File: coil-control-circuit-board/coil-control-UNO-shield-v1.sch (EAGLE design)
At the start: 26 parts, among them Q1 IRLML0060, Q2 IRLML0060, SW2 BUTTON, SW3 BUTTON, U2 LM4250, U3 LM4250

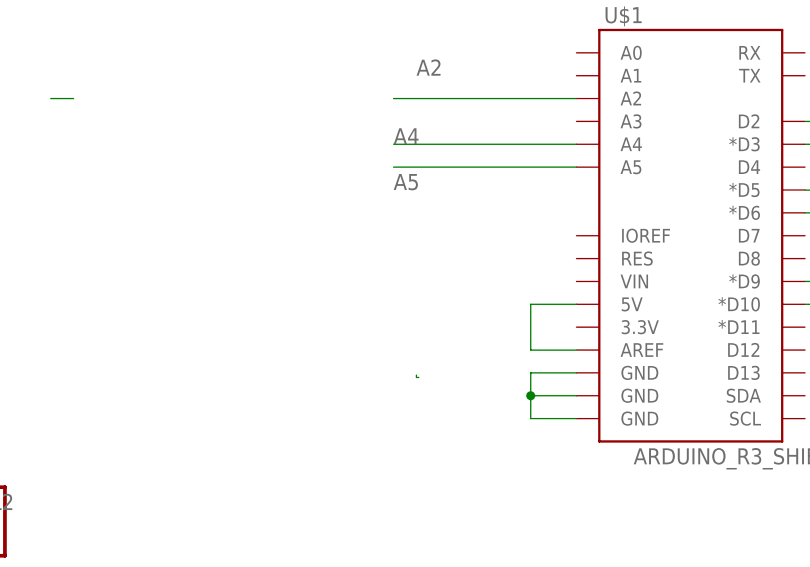
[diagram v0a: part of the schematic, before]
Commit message: finished the boards, mostly
added DC power connector, shifted everything over to work on the Yun(
make space for the big connectors), connected Vin to the input DC
power, cleaned stuff up a bit, moved stuff around.
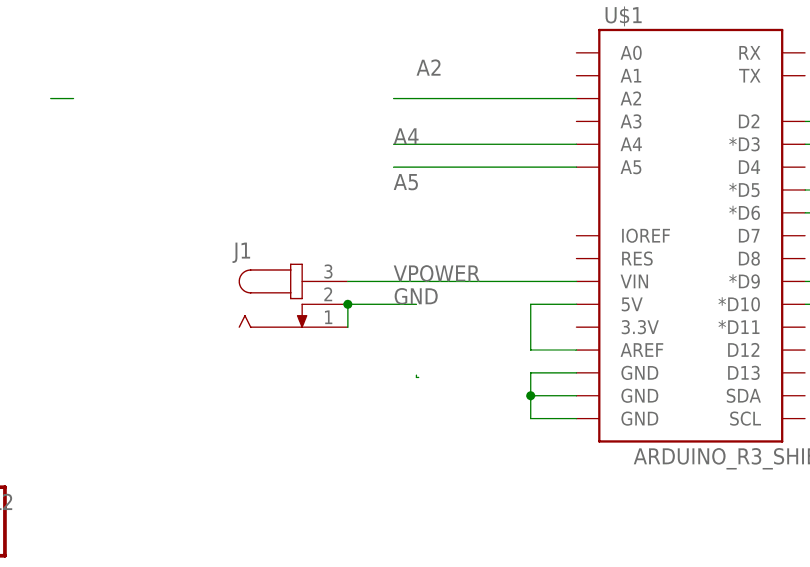
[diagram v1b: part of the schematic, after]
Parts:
- added J1: (no value), con-jack:JACK-PLUG1
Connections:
- net GND: now also J1.1, J1.2
- net VPOWER: now also J1.3, U$1.VIN
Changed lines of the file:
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@@
 <setting verticaltext="up"/>
 </settings>
-<grid distance="0.1" unitdist="inch" unit="inch" style="lines" multiple="1" display="yes" altdistance="0.01" altunitdist="inch" altunit="inch"/>
+<grid distance="0.01" unitdist="inch" unit="inch" style="lines" multiple="1" display="yes" altdistance="0.01" altunitdist="inch" altunit="inch"/>
 <layers>
 <layer number="1" name="Top" color="4" fill="1" visible="no" active="no"/>
@@
 <part name="R12" library="SparkFun-Passives" deviceset="RESISTOR" device="0805-RES" value="1M"/>
 <part name="U$1" library="SparkFun-Boards" deviceset="ARDUINO_R3_SHIELD" device=""/>
+<part name="J1" library="con-jack" deviceset="JACK-PLUG" device="1"/>
 </parts>
 <sheets>
@@
 <instance part="R12" gate="G$1" x="129.286" y="117.602"/>
 <instance part="U$1" gate="G$1" x="220.98" y="121.92"/>
+<instance part="J1" gate="G$1" x="177.8" y="111.76"/>
 </instances>
 <busses>
@@
 <junction x="203.2" y="101.6"/>
 </segment>
+<segment>
+<pinref part="J1" gate="G$1" pin="1"/>
+<pinref part="J1" gate="G$1" pin="2"/>
+<wire x1="182.88" y1="109.22" x2="182.88" y2="111.76" width="0.1524" layer="91"/>
+<wire x1="182.88" y1="111.76" x2="190.5" y2="111.76" width="0.1524" layer="91"/>
+<junction x="182.88" y="111.76"/>
+<label x="187.96" y="111.76" size="1.778" layer="95"/>
+</segment>
 </net>
 <net name="VCC" class="0">
@@
 <pinref part="JP5" gate="G$1" pin="1"/>
 </segment>
+<segment>
+<pinref part="J1" gate="G$1" pin="3"/>
+<label x="187.96" y="114.3" size="1.778" layer="95"/>
+<wire x1="182.88" y1="114.3" x2="208.28" y2="114.3" width="0.1524" layer="91"/>
+<pinref part="U$1" gate="G$1" pin="VIN"/>
+</segment>
 </net>
